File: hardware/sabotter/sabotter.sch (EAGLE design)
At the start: 96 parts, among them IC1 MAX3232CSE, IC2 MAX3232CSE, IC3 OKI-78SR-3.3/1.5-W36H-C, IC4 OKI-78SR-5/1.5-W36H-C, IC6 ATXMEGA256A3U-AU

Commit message: add audio amplifier
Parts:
- added C27, C29: 1UF_50V_1206, robotter_capacitor:C_1UF
- added C28, C30: C_10UF, robotter_capacitor:C_10UF
- added C31: 100NF_50V_0805, robotter_capacitor:C_100NF
- added HP: 1503_04, con-lumberg:1503_04
- added IC7: LM4871M, robotter_ic:LM4871M
- added R24, R25, R37, R38: 10K-F, robotter_resistor:10K-F
- C13, C14, C15, C16, C2: value 10UF35V-C -> 10UFC; device robotter_capacitor:10UF35V-C -> robotter_capacitor:10UFC
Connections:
- new net AUDIO_PWM_3V3: IC6.PD0/OC0A, R24.1
- new net ENABLE_AUDIO_OUPUT_3V3: IC6.PD1/OC0B/XCK0, IC7.SHUTDOWN, R38.2
- new net N$15: C29.2, IC7.+IN, IC7.BYPASS
- new net N$20: C27.1, C28.2, R24.2
- new net N$36: C27.2, R25.1
- new net N$37: IC7.-IN, R25.2, R37.1
- new net N$38: IC7.VO1, R37.2
- net +5V: now also C30.1, C31.1, IC7.VDD
- net GND: now also C28.1, C29.1, C30.2, C31.2, IC7.GND, R38.1
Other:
- note added: "manque connection connecteur jack"
- note added: "rename UART"
- note added: "todo connect leds"
- note removed: "manque connecteur alim"
- note removed: "manque connecteur pour tirette"
- moved on the sheet: R2, R3

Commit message: board ready for eirbot assembly
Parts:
- removed LED2, LED3, LED4, LED5: GREEN_0805, robotter_diode:LED_G
- added LA1, LA2, LA3, LA4: GREEN_0805, robotter_diode:LED_G
- added R39, R40, R41, R42: 10K-F, robotter_resistor:10K-F
- renumbered UART_A4 to UART_E0, UART_A5 to UART_D0, UART_A6 to UART_C0
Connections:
- net RX_A4_232 renamed RX_E0_232
- net RX_A5_232 renamed RX_D0_232
- net RX_A6_232 renamed RX_C0_232
- net TX_A4_232 renamed TX_E0_232
- net TX_A4_3V3 renamed TX_E0_3V3
- net TX_A5_232 renamed TX_D0_232
- net TX_A5_3V3 renamed TX_D0_3V3
- net TX_A6_232 renamed TX_C0_232
- net TX_A6_3V3 renamed TX_C0_3V3
- removed net N$10: LED4.A
- removed net N$11: LED7.C, R9.2
- removed net N$12: LED5.A
- removed net N$74: IC6.PA3/ADCA3
- removed net N$77: IC6.PA4/ADCA4
- removed net N$78: IC6.PA5/ADCA5
- removed net N$79: IC6.PA6/ADCA6
- removed net N$80: IC6.PA7/ADCA7
- removed net N$9: LED3.A
- removed net RX_A4_3V3: IC1G$1.R1OUT, IC6.RXD0/OC0C/PE2, R26.2
- removed net RX_A5_3V3: IC2G$1.R1OUT, IC6.PD2/OC0C/RXD0, R27.2
- removed net RX_A6_3V3: IC2G$1.R2OUT, IC6.PC2/OC0C/RXD0, R28.2
- new net LA1: IC6.PA1/ADCA1, R5.2
- new net LA2: IC6.PA2/ADCA2, R4.2
- new net LA3: IC6.PA3/ADCA3, R7.2
- new net LA4: IC6.PA4/ADCA4, R6.2
- new net RX_C0_3V3: IC2G$1.R2OUT, IC6.PC2/OC0C/RXD0, R28.2, R39.2
- new net RX_D0_3V3: IC2G$1.R1OUT, IC6.PD2/OC0C/RXD0, R27.2, R40.2
- new net RX_E0_3V3: IC1G$1.R1OUT, IC6.RXD0/OC0C/PE2, R26.2, R41.2
- net GND: now also LA1.C, LA2.C, LA3.C, LA4.C, LED6.C, LED7.C, LED8.C, LED9.C, R39.1, R40.1, R41.1, R42.1; no longer R10.1, R11.1, R4.1, R5.1, R6.1, R7.1, R8.1, R9.1
- net N$1: now also LA2.A, R4.1; no longer LED2.C, R4.2
- net N$13: now also R8.2; no longer LED6.A
- net N$14: now also R9.2; no longer LED7.A
- net N$16: now also R10.2; no longer LED8.A
- net N$17: now also R11.2; no longer LED9.A
- net N$2: now also LA1.A, R5.1; no longer LED3.C, R5.2
- net N$3: now also LED6.A, R8.1; no longer LED4.C, R6.2
- net N$4: now also LA3.A, R7.1; no longer LED5.C, R7.2
- net N$5: now also LED7.A, R9.1; no longer LED6.C, R8.2
- net N$6: now also LED8.A, R10.1; no longer LED8.C, R10.2
- net N$7: now also LED9.A, R11.1; no longer LED9.C, R11.2
- net N$8: now also LA4.A, R6.1; no longer LED2.A
- net RX_PROP_3V3: now also R42.2
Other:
- note removed: "manque R tirage gnd sur lignes RX"
- note removed: "rename UART"
- moved on the sheet: LED6, LED7, LED8, LED9, R10, R11, R4, R5, R6, R7, R8, R9

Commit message: board ready for eirbot assembly, sabotter V1
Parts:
- HP: value 1503_04 -> 1503_12"; device con-lumberg:1503_04 -> robotter_connector:1503_12"
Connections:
- net N$13 renamed LED4
- net N$14 renamed LED3
- net N$16 renamed LED2
- net N$17 renamed LED1
- new net N$9: HP.5, IC7.VO2
- net N$38: now also HP.3, HP.4
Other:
- moved on the sheet: HP
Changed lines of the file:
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@@
 <part name="COLOR/START" library="robotter_connector" deviceset="794618-4" device=""/>
 <part name="GND14" library="supply1" deviceset="GND" device=""/>
-<part name="HP" library="con-lumberg" deviceset="1503_04" device=""/>
+<part name="HP" library="robotter_connector" deviceset="1503_12" device="&quot;"/>
 <part name="FRAME8" library="frames" deviceset="A4L-LOC" device=""/>
 <part name="R24" library="robotter_resistor" deviceset="10K" device="-F"/>
@@
 <instance part="COLOR/START" gate="G$1" x="101.6" y="-414.02"/>
 <instance part="GND14" gate="1" x="93.98" y="-421.64"/>
-<instance part="HP" gate="G$1" x="472.44" y="-434.34"/>
+<instance part="HP" gate="G$1" x="434.34" y="-447.04"/>
 <instance part="FRAME8" gate="G$1" x="261.62" y="-541.02"/>
 <instance part="R24" gate="G$1" x="314.96" y="-434.34"/>
@@
 </segment>
 </net>
-<net name="N$13" class="0">
+<net name="LED4" class="0">
 <segment>
 <wire x1="109.22" y1="-91.44" x2="40.64" y2="-91.44" width="0.1524" layer="91"/>
@@
 </segment>
 </net>
-<net name="N$14" class="0">
+<net name="LED3" class="0">
 <segment>
 <wire x1="119.38" y1="-88.9" x2="40.64" y2="-88.9" width="0.1524" layer="91"/>
@@
 </segment>
 </net>
-<net name="N$16" class="0">
+<net name="LED2" class="0">
 <segment>
 <wire x1="129.54" y1="-86.36" x2="40.64" y2="-86.36" width="0.1524" layer="91"/>
@@
 </segment>
 </net>
-<net name="N$17" class="0">
+<net name="LED1" class="0">
 <segment>
 <wire x1="139.7" y1="-83.82" x2="40.64" y2="-83.82" width="0.1524" layer="91"/>
@@
 <pinref part="IC7" gate="G$1" pin="VO1"/>
 <wire x1="429.26" y1="-439.42" x2="398.78" y2="-439.42" width="0.1524" layer="91"/>
+<pinref part="HP" gate="G$1" pin="4"/>
+<pinref part="HP" gate="G$1" pin="3"/>
+<wire x1="429.26" y1="-447.04" x2="429.26" y2="-444.5" width="0.1524" layer="91"/>
+<wire x1="429.26" y1="-444.5" x2="429.26" y2="-439.42" width="0.1524" layer="91"/>
+<junction x="429.26" y="-444.5"/>
+<junction x="429.26" y="-439.42"/>
 </segment>
 </net>
@@
 </segment>
 </net>
+<net name="N$9" class="0">
+<segment>
+<pinref part="IC7" gate="G$1" pin="VO2"/>
+<wire x1="398.78" y1="-449.58" x2="429.26" y2="-449.58" width="0.1524" layer="91"/>
+<pinref part="HP" gate="G$1" pin="5"/>
+</segment>
+</net>

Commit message: leds connected to µC, board ready for industrial assembly, sabotter V2
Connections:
- net LA1 renamed LA1_3V3
- net LA2 renamed LA2_3V3
- net LA3 renamed LA3_3V3
- net LA4 renamed LA4_3V3
- removed net LED1: R11.2
- removed net LED2: R10.2
- removed net LED3: R9.2
- removed net LED4: R8.2
- removed net N$112: IC6.PF7
- removed net N$54: R12.1, R17.2
- removed net N$55: R13.1, R16.2
- removed net N$56: R14.1, R15.2
- removed net N$81: IC6.PB0/ADCB0/AREF
- removed net N$82: IC6.PB1/ADCB1
- removed net N$83: IC6.PB2/ADCB2/DAC0
- removed net N$84: IC6.PB3/ADCB3/DAC1
- removed net N$85: IC6.PB4/ADCB4/TMS
- removed net N$86: IC6.PB5/ADCB5/TDI
- removed net N$87: IC6.PB6/ADCB6/TCK
- new net LB3_3V3: IC6.PB3/ADCB3/DAC1, R8.2
- new net LB4_3V3: IC6.PB4/ADCB4/TMS, R9.2
- new net LB5_3V3: IC6.PB5/ADCB5/TDI, R10.2
- new net LB6_3V3: IC6.PB6/ADCB6/TCK, R11.2
- new net LED_BLUE_3V3: IC6.PA7/ADCA7, R12.1, R17.2
- new net LED_GREEN_3V3: IC6.PF7, R13.1, R16.2
- new net LED_RED_3V3: IC6.OC0A/PF0, R14.1, R15.2
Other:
- note removed: "manque connection connecteur jack"
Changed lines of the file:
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@@
 <text x="7.62" y="-373.38" size="5.08" layer="91">User interface</text>
 <text x="10.16" y="-106.68" size="1.778" layer="91">todo connect leds</text>
-<text x="429.26" y="-462.28" size="1.778" layer="91">manque connection connecteur jack</text>
 </plain>
 <instances>
@@
 </segment>
 </net>
-<net name="LA4" class="0">
+<net name="LA4_3V3" class="0">
 <segment>
 <wire x1="40.64" y1="-96.52" x2="88.9" y2="-96.52" width="0.1524" layer="91"/>
@@
 </segment>
 </net>
-<net name="LA3" class="0">
+<net name="LA3_3V3" class="0">
 <segment>
 <wire x1="40.64" y1="-93.98" x2="99.06" y2="-93.98" width="0.1524" layer="91"/>
@@
 <wire x1="27.94" y1="124.46" x2="58.42" y2="124.46" width="0.1524" layer="91"/>
 <label x="27.94" y="124.46" size="1.778" layer="95"/>
-</segment>
-</net>
-<net name="LED4" class="0">
-<segment>
-<wire x1="109.22" y1="-91.44" x2="40.64" y2="-91.44" width="0.1524" layer="91"/>
-<label x="40.64" y="-91.44" size="1.778" layer="95"/>
-<pinref part="R8" gate="G$1" pin="2"/>
-</segment>
-</net>
-<net name="LED3" class="0">
-<segment>
-<wire x1="119.38" y1="-88.9" x2="40.64" y2="-88.9" width="0.1524" layer="91"/>
-<label x="40.64" y="-88.9" size="1.778" layer="95"/>
-<pinref part="R9" gate="G$1" pin="2"/>
-</segment>
-</net>
-<net name="LED2" class="0">
-<segment>
-<wire x1="129.54" y1="-86.36" x2="40.64" y2="-86.36" width="0.1524" layer="91"/>
-<label x="40.64" y="-86.36" size="1.778" layer="95"/>
-<pinref part="R10" gate="G$1" pin="2"/>
-</segment>
-</net>
-<net name="LED1" class="0">
-<segment>
-<wire x1="139.7" y1="-83.82" x2="40.64" y2="-83.82" width="0.1524" layer="91"/>
-<label x="40.64" y="-83.82" size="1.778" layer="95"/>
-<pinref part="R11" gate="G$1" pin="2"/>
 </segment>
 </net>
@@
 <pinref part="T1" gate="G$1" pin="B"/>
 <wire x1="88.9" y1="-58.42" x2="91.44" y2="-58.42" width="0.1524" layer="91"/>
-</segment>
-</net>
-<net name="N$55" class="0">
-<segment>
-<pinref part="R13" gate="G$1" pin="1"/>
-<wire x1="40.64" y1="-50.8" x2="66.04" y2="-50.8" width="0.1524" layer="91"/>
-<pinref part="R16" gate="G$1" pin="2"/>
-<wire x1="66.04" y1="-50.8" x2="78.74" y2="-50.8" width="0.1524" layer="91"/>
-<wire x1="66.04" y1="-60.96" x2="66.04" y2="-50.8" width="0.1524" layer="91"/>
-<junction x="66.04" y="-50.8"/>
-<label x="40.64" y="-50.8" size="1.778" layer="95"/>
-</segment>
-</net>
-<net name="N$56" class="0">
-<segment>
-<pinref part="R14" gate="G$1" pin="1"/>
-<wire x1="78.74" y1="-43.18" x2="76.2" y2="-43.18" width="0.1524" layer="91"/>
-<pinref part="R15" gate="G$1" pin="2"/>
-<wire x1="76.2" y1="-43.18" x2="40.64" y2="-43.18" width="0.1524" layer="91"/>
-<wire x1="76.2" y1="-60.96" x2="76.2" y2="-43.18" width="0.1524" layer="91"/>
-<junction x="76.2" y="-43.18"/>
-<label x="40.64" y="-43.18" size="1.778" layer="95"/>
-</segment>
-</net>
-<net name="N$54" class="0">
-<segment>
-<pinref part="R12" gate="G$1" pin="1"/>
-<wire x1="78.74" y1="-58.42" x2="55.88" y2="-58.42" width="0.1524" layer="91"/>
-<pinref part="R17" gate="G$1" pin="2"/>
-<wire x1="55.88" y1="-58.42" x2="40.64" y2="-58.42" width="0.1524" layer="91"/>
-<wire x1="55.88" y1="-60.96" x2="55.88" y2="-58.42" width="0.1524" layer="91"/>
-<junction x="55.88" y="-58.42"/>
-<label x="40.64" y="-58.42" size="1.778" layer="95"/>
 </segment>
 </net>
@@
 </segment>
 </net>
-<net name="N$81" class="0">
-<segment>
-<wire x1="58.42" y1="109.22" x2="27.94" y2="109.22" width="0.1524" layer="91"/>
-<pinref part="IC6" gate="G$1" pin="PB0/ADCB0/AREF"/>
-</segment>
-</net>
-<net name="N$82" class="0">
-<segment>
-<wire x1="27.94" y1="106.68" x2="58.42" y2="106.68" width="0.1524" layer="91"/>
-<pinref part="IC6" gate="G$1" pin="PB1/ADCB1"/>
-</segment>
-</net>
-<net name="N$83" class="0">
-<segment>
-<wire x1="58.42" y1="104.14" x2="27.94" y2="104.14" width="0.1524" layer="91"/>
-<pinref part="IC6" gate="G$1" pin="PB2/ADCB2/DAC0"/>
-</segment>
-</net>
-<net name="N$84" class="0">
-<segment>
-<wire x1="27.94" y1="101.6" x2="58.42" y2="101.6" width="0.1524" layer="91"/>
-<pinref part="IC6" gate="G$1" pin="PB3/ADCB3/DAC1"/>
-</segment>
-</net>
-<net name="N$85" class="0">
-<segment>
-<wire x1="58.42" y1="99.06" x2="27.94" y2="99.06" width="0.1524" layer="91"/>
-<pinref part="IC6" gate="G$1" pin="PB4/ADCB4/TMS"/>
-</segment>
-</net>
-<net name="N$86" class="0">
-<segment>
-<wire x1="27.94" y1="96.52" x2="58.42" y2="96.52" width="0.1524" layer="91"/>
-<pinref part="IC6" gate="G$1" pin="PB5/ADCB5/TDI"/>
-</segment>
-</net>
-<net name="N$87" class="0">
-<segment>
-<wire x1="58.42" y1="93.98" x2="27.94" y2="93.98" width="0.1524" layer="91"/>
-<pinref part="IC6" gate="G$1" pin="PB6/ADCB6/TCK"/>
-</segment>
-</net>
-<net name="N$112" class="0">
-<segment>
-<wire x1="121.92" y1="83.82" x2="152.4" y2="83.82" width="0.1524" layer="91"/>
-<pinref part="IC6" gate="G$1" pin="PF7"/>
-</segment>
-</net>
 <net name="N$15" class="0">
 <segment>
@@
 </segment>
 </net>
-<net name="LA1" class="0">
+<net name="LA1_3V3" class="0">
 <segment>
 <pinref part="IC6" gate="G$1" pin="PA1/ADCA1"/>
@@
 </segment>
 </net>
-<net name="LA2" class="0">
+<net name="LA2_3V3" class="0">
 <segment>
 <pinref part="IC6" gate="G$1" pin="PA2/ADCA2"/>
@@
 </segment>
 </net>
+<net name="LB3_3V3" class="0">
+<segment>
+<wire x1="109.22" y1="-91.44" x2="40.64" y2="-91.44" width="0.1524" layer="91"/>
+<label x="40.64" y="-91.44" size="1.778" layer="95"/>
+<pinref part="R8" gate="G$1" pin="2"/>
+</segment>
+<segment>
+<wire x1="27.94" y1="101.6" x2="58.42" y2="101.6" width="0.1524" layer="91"/>
+<pinref part="IC6" gate="G$1" pin="PB3/ADCB3/DAC1"/>
+<label x="27.94" y="101.6" size="1.778" layer="95"/>
+</segment>
+</net>
+<net name="LB4_3V3" class="0">
+<segment>
+<wire x1="119.38" y1="-88.9" x2="40.64" y2="-88.9" width="0.1524" layer="91"/>
+<label x="40.64" y="-88.9" size="1.778" layer="95"/>
+<pinref part="R9" gate="G$1" pin="2"/>
+</segment>
+<segment>
+<wire x1="58.42" y1="99.06" x2="27.94" y2="99.06" width="0.1524" layer="91"/>
+<pinref part="IC6" gate="G$1" pin="PB4/ADCB4/TMS"/>
+<label x="27.94" y="99.06" size="1.778" layer="95"/>
+</segment>
+</net>
+<net name="LB5_3V3" class="0">
+<segment>
+<wire x1="129.54" y1="-86.36" x2="40.64" y2="-86.36" width="0.1524" layer="91"/>
+<label x="40.64" y="-86.36" size="1.778" layer="95"/>
+<pinref part="R10" gate="G$1" pin="2"/>
+</segment>
+<segment>
+<wire x1="27.94" y1="96.52" x2="58.42" y2="96.52" width="0.1524" layer="91"/>
+<pinref part="IC6" gate="G$1" pin="PB5/ADCB5/TDI"/>
+<label x="27.94" y="96.52" size="1.778" layer="95"/>
+</segment>
+</net>
+<net name="LB6_3V3" class="0">
+<segment>
+<wire x1="139.7" y1="-83.82" x2="40.64" y2="-83.82" width="0.1524" layer="91"/>
+<label x="40.64" y="-83.82" size="1.778" layer="95"/>
+<pinref part="R11" gate="G$1" pin="2"/>
+</segment>
+<segment>
+<wire x1="58.42" y1="93.98" x2="27.94" y2="93.98" width="0.1524" layer="91"/>
+<pinref part="IC6" gate="G$1" pin="PB6/ADCB6/TCK"/>
+<label x="27.94" y="93.98" size="1.778" layer="95"/>
+</segment>
+</net>
+<net name="LED_RED_3V3" class="0">
+<segment>
+<pinref part="R14" gate="G$1" pin="1"/>
+<wire x1="78.74" y1="-43.18" x2="76.2" y2="-43.18" width="0.1524" layer="91"/>
+<pinref part="R15" gate="G$1" pin="2"/>
+<wire x1="76.2" y1="-43.18" x2="40.64" y2="-43.18" width="0.1524" layer="91"/>
+<wire x1="76.2" y1="-60.96" x2="76.2" y2="-43.18" width="0.1524" layer="91"/>
+<junction x="76.2" y="-43.18"/>
+<label x="40.64" y="-43.18" size="1.778" layer="95"/>
+</segment>
+<segment>
+<pinref part="IC6" gate="G$1" pin="OC0A/PF0"/>
+<wire x1="121.92" y1="101.6" x2="152.4" y2="101.6" width="0.1524" layer="91"/>
+</segment>
+</net>
+<net name="LED_GREEN_3V3" class="0">
+<segment>
+<pinref part="R13" gate="G$1" pin="1"/>
+<wire x1="40.64" y1="-50.8" x2="66.04" y2="-50.8" width="0.1524" layer="91"/>
+<pinref part="R16" gate="G$1" pin="2"/>
+<wire x1="66.04" y1="-50.8" x2="78.74" y2="-50.8" width="0.1524" layer="91"/>
+<wire x1="66.04" y1="-60.96" x2="66.04" y2="-50.8" width="0.1524" layer="91"/>
+<junction x="66.04" y="-50.8"/>
+<label x="40.64" y="-50.8" size="1.778" layer="95"/>
+</segment>
+<segment>
+<pinref part="IC6" gate="G$1" pin="PF7"/>
+<wire x1="121.92" y1="83.82" x2="152.4" y2="83.82" width="0.1524" layer="91"/>
+</segment>
+</net>
+<net name="LED_BLUE_3V3" class="0">
+<segment>
+<pinref part="IC6" gate="G$1" pin="PA7/ADCA7"/>
+<wire x1="58.42" y1="114.3" x2="27.94" y2="114.3" width="0.1524" layer="91"/>
+<label x="30.48" y="114.3" size="1.778" layer="95"/>
+</segment>
+<segment>
+<pinref part="R12" gate="G$1" pin="1"/>
+<wire x1="78.74" y1="-58.42" x2="55.88" y2="-58.42" width="0.1524" layer="91"/>
+<pinref part="R17" gate="G$1" pin="2"/>
+<wire x1="55.88" y1="-58.42" x2="40.64" y2="-58.42" width="0.1524" layer="91"/>
+<wire x1="55.88" y1="-60.96" x2="55.88" y2="-58.42" width="0.1524" layer="91"/>
+<junction x="55.88" y="-58.42"/>
+<label x="40.64" y="-58.42" size="1.778" layer="95"/>
+</segment>
+</net>

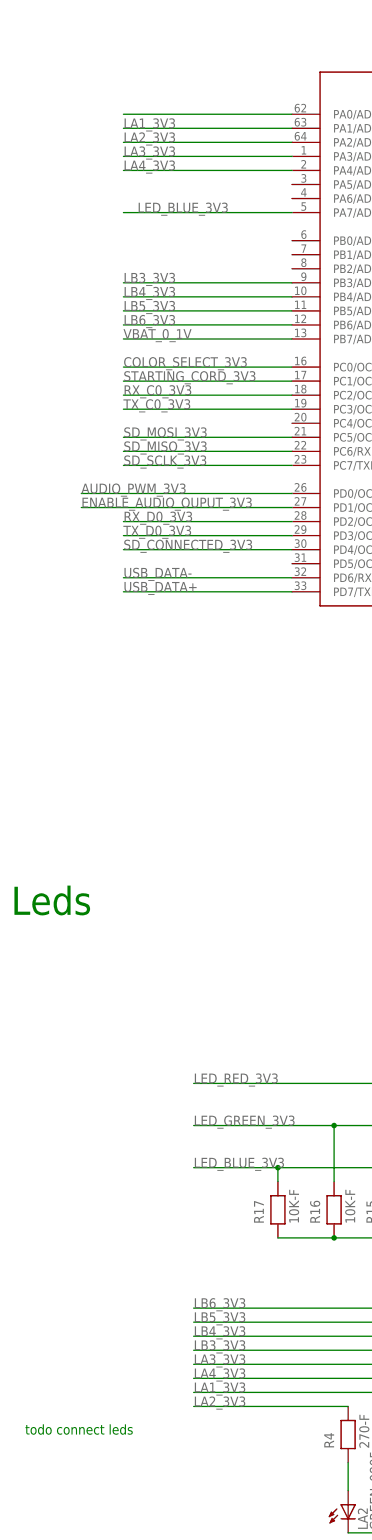
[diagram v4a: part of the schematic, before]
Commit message: led inverted, now in ascending order
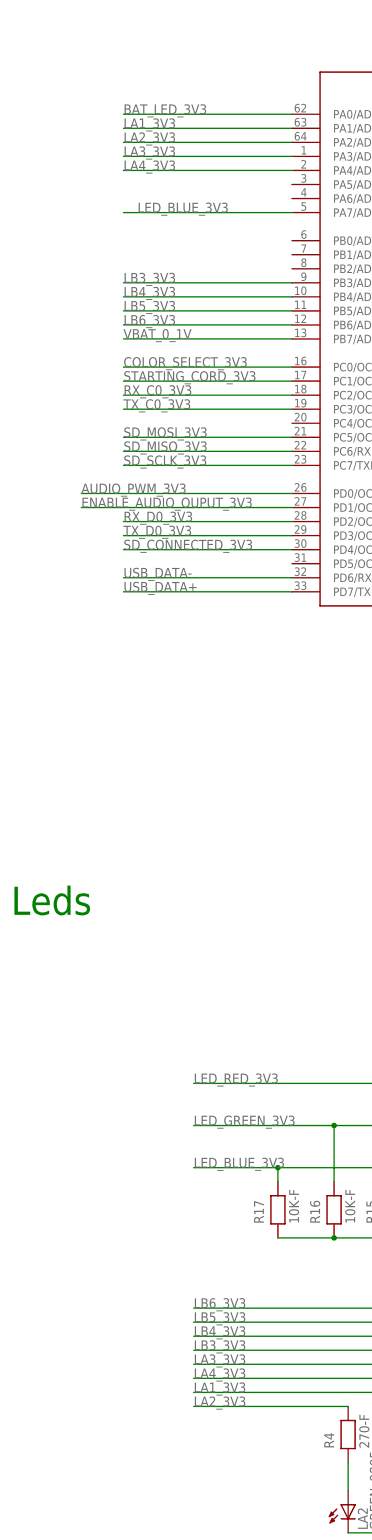
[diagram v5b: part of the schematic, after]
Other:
- note removed: "todo connect leds"
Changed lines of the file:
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@@
 <text x="269.24" y="-193.04" size="5.08" layer="91">Super Unioc connectors</text>
 <text x="7.62" y="-373.38" size="5.08" layer="91">User interface</text>
-<text x="10.16" y="-106.68" size="1.778" layer="91">todo connect leds</text>
 </plain>
 <instances>
@@
 <pinref part="IC6" gate="G$1" pin="PA0/ADCA0/AREF"/>
 <wire x1="58.42" y1="132.08" x2="27.94" y2="132.08" width="0.1524" layer="91"/>
-</segment>
-</net>
+<label x="27.94" y="132.08" size="1.778" layer="95"/>
+</segment>
+</net>

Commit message: sabotter: uart modified after Jdam  peer review
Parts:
- added C32: C_10UF, robotter_capacitor:C_10UF
- R24: value 10K-F -> 470; device robotter_resistor:10K-F -> robotter_resistor:470-F
- R33: value (none) -> 10M
- T1, T2, T3: value (none) -> 2n2222
- renumbered LED6 to LB3, LED7 to LB4, LED8 to LB5, LED9 to LB6
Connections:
- removed net N$19: C10.1, IC1G$1.V-
- removed net PD4: JB2.9
- removed net PD5: JB2.10
- removed net PD6: JB2.8
- removed net PD7: JB2.7
- new net V-: C10.1, IC1G$1.R2IN, IC1G$1.V-
- net AUDIO_PWM_3V3: now also IC6.PB2/ADCB2/DAC0
- net GND: now also C32.2; no longer IC1G$1.T1OUT
- net TX_C0_232: now also IC2G$1.T2OUT; no longer IC2G$1.T2IN
- net TX_C0_3V3: now also IC2G$1.T2IN; no longer IC2G$1.T2OUT
- net TX_D0_232: now also IC2G$1.T1OUT; no longer IC2G$1.T1IN
- net TX_D0_3V3: now also IC2G$1.T1IN; no longer IC2G$1.T1OUT
- net TX_E0_232: now also IC1G$1.T2OUT; no longer IC1G$1.R2IN, IC1G$1.T2IN
- net TX_E0_3V3: now also IC1G$1.T1IN, IC1G$1.T2IN; no longer IC1G$1.T2OUT
- net VBAT_0_1V: now also C32.1
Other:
- note added: "WARNING : audio_pwm_3v3 connected both on pwm pin and on dac pin, take care to specify unused pin as input"
- moved on the sheet: C10, C11
